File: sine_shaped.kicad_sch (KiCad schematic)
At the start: 14 parts, among them Q1 NPN, Q2 NPN, U3 ${SIM.PARAMS}

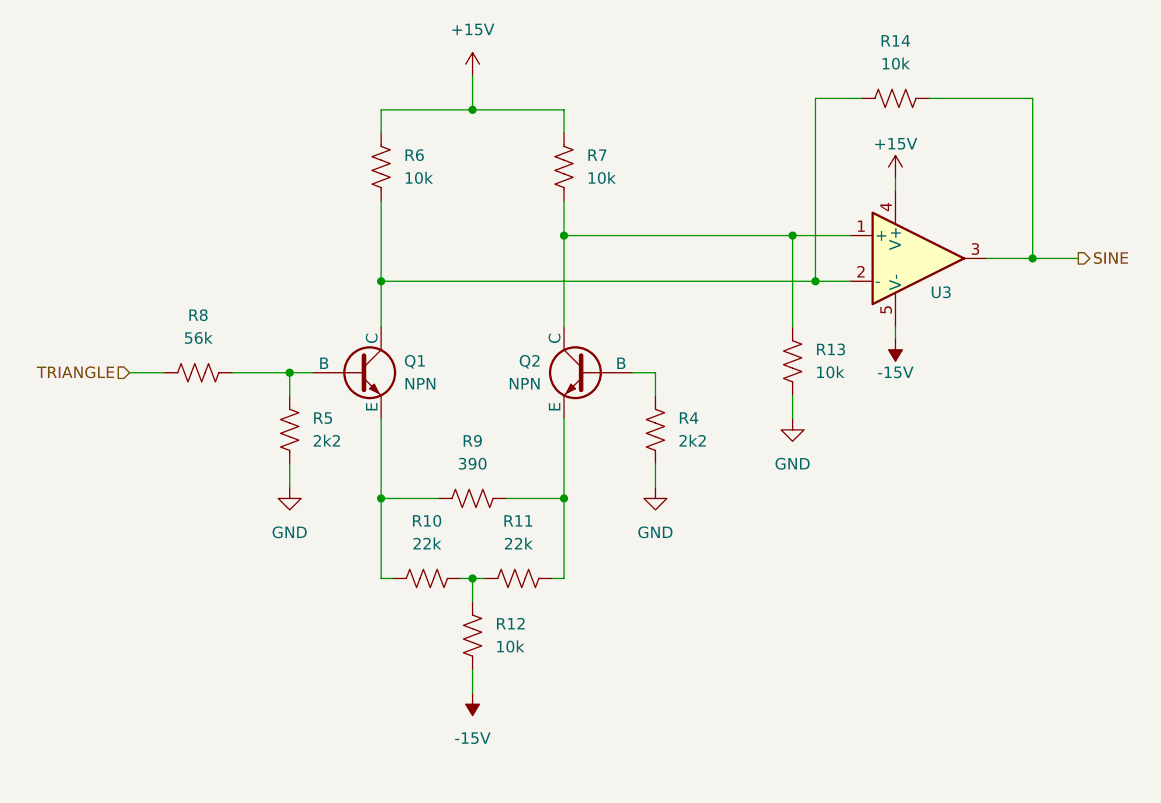
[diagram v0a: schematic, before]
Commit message: added spice model and reworked output stage
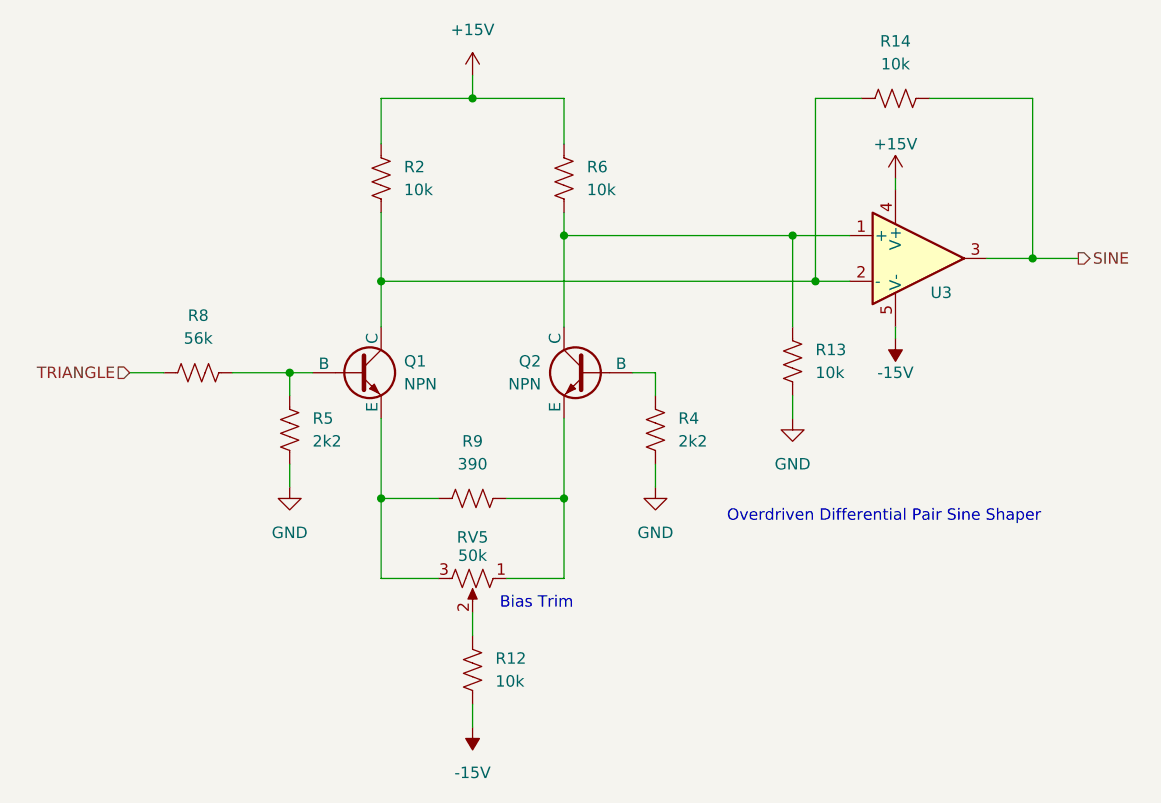
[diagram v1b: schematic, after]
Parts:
- removed R10, R11: 22k, symbol Device:R_US
- removed R7: 10k, symbol Device:R_US
- added R2: 10k, symbol Device:R_US
- added RV5: 50k, symbol Device:R_Potentiometer_US
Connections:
- net +15V: now also R6.2, R2.2; no longer R6.1
- net at Q2.1 (C), R13.1, U3.1 (+): now also R6.1
- net at R12.1: now also RV5.2
- net at Q2.3 (E), R9.2: now also RV5.1
- net at Q1.1 (C), R14.1, U3.2 (-): now also R2.1; no longer R6.2
- net at Q1.3 (E), R9.1: now also RV5.3
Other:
- note added: "Bias Trim"
- note added: "Overdriven Differential Pair Sine Shaper"
- moved on the sheet: R12
